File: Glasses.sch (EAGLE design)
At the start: 7 parts, among them U1 APA1022020, U2 APA1022020, U3 APA1022020, U4 APA1022020, U5 APA1022020, U6 APA1022020

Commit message: laid out LED's
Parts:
- added FRAME2, FRAME3, FRAME4, FRAME5, FRAME6, FRAME7: FRAME-LETTERNO_PACKAGE, SparkFun-Aesthetics:FRAME-LETTERNO_PACKAGE
- added U10, U100, U101, U102, U103, U104, U105, U106, U107, U108, U109, U11, U110, U111, U112, U113, U114, U115, U116, U117, U118, U119, U12, U120, U121, U122, U123, U124, U125, U126, U127, U128, U129, U13, U130, U131, U132, U133, U134, U135, U136, U137, U138, U139, U14, U140, U141, U142, U143, U144, U145, U146, U147, U148, U149, U15, U150, U151, U152, U153, U154, U155, U156, U157, U158, U159, U16, U160, U161, U162, U163, U164, U165, U166, U167, U168, U169, U17, U170, U171, U172, U173, U174, U175, U176, U177, U178, U179, U18, U180, U181, U182, U183, U184, U185, U186, U187, U188, U189, U19, U190, U20, U21, U22, U23, U24, U25, U26, U27, U28, U29, U30, U31, U32, U33, U34, U35, U36, U37, U38, U39, U40, U41, U42, U43, U44, U45, U46, U47, U48, U49, U50, U51, U52, U53, U54, U55, U56, U57, U58, U59, U60, U61, U62, U63, U64, U65, U66, U67, U68, U69, U7, U70, U71, U72, U73, U74, U75, U76, U77, U78, U79, U8, U80, U81, U82, U83, U84, U85, U86, U87, U88, U89, U9, U90, U91, U92, U93, U94, U95, U96, U97, U98, U99: APA1022020, 1_BES_Optoelectronics:APA1022020
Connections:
- new net CK1: U28.CO, U29.CI
- new net CK2: U56.CO, U57.CI
- new net CK3: U84.CO, U85.CI
- new net CK4: U112.CO, U113.CI
- new net CK5: U140.CO, U141.CI
- new net CK6: U168.CO, U169.CI
- new net N$100: U53.DO, U54.DI
- new net N$101: U54.CO, U55.CI
- new net N$102: U54.DO, U55.DI
- new net N$103: U55.CO, U56.CI
- new net N$104: U55.DO, U56.DI
- new net N$105: U49.DO, U50.DI
- new net N$106: U49.CO, U50.CI
- new net N$107: U42.DO, U43.DI
- new net N$108: U42.CO, U43.CI
- new net N$109: U57.DO, U58.DI
- new net N$11: U6.CO, U7.CI
- new net N$110: U57.CO, U58.CI
- new net N$111: U58.CO, U59.CI
- new net N$112: U58.DO, U59.DI
- new net N$113: U59.DO, U60.DI
- new net N$114: U59.CO, U60.CI
- new net N$115: U60.CO, U61.CI
- new net N$116: U60.DO, U61.DI
- new net N$117: U61.CO, U62.CI
- new net N$118: U61.DO, U62.DI
- new net N$119: U62.CO, U63.CI
- new net N$12: U6.DO, U7.DI
- new net N$120: U62.DO, U63.DI
- new net N$121: U64.DO, U65.DI
- new net N$122: U64.CO, U65.CI
- new net N$123: U65.CO, U66.CI
- new net N$124: U65.DO, U66.DI
- new net N$125: U66.DO, U67.DI
- new net N$126: U66.CO, U67.CI
- new net N$127: U67.CO, U68.CI
- new net N$128: U67.DO, U68.DI
- new net N$129: U68.CO, U69.CI
- new net N$13: U8.DO, U9.DI
- new net N$130: U68.DO, U69.DI
- new net N$131: U69.CO, U70.CI
- new net N$132: U69.DO, U70.DI
- new net N$133: U63.DO, U64.DI
- new net N$134: U63.CO, U64.CI
- new net N$135: U71.DO, U72.DI
- new net N$136: U71.CO, U72.CI
- new net N$137: U72.CO, U73.CI
- new net N$138: U72.DO, U73.DI
- new net N$139: U73.DO, U74.DI
- new net N$14: U8.CO, U9.CI
- new net N$140: U73.CO, U74.CI
- new net N$141: U74.CO, U75.CI
- new net N$142: U74.DO, U75.DI
- new net N$143: U75.CO, U76.CI
- new net N$144: U75.DO, U76.DI
- new net N$145: U76.CO, U77.CI
- new net N$146: U76.DO, U77.DI
- new net N$147: U78.DO, U79.DI
- new net N$148: U78.CO, U79.CI
- new net N$149: U79.CO, U80.CI
- new net N$15: U10.CI, U9.CO
- new net N$150: U79.DO, U80.DI
- new net N$151: U80.DO, U81.DI
- new net N$152: U80.CO, U81.CI
- new net N$153: U81.CO, U82.CI
- new net N$154: U81.DO, U82.DI
- new net N$155: U82.CO, U83.CI
- new net N$156: U82.DO, U83.DI
- new net N$157: U83.CO, U84.CI
- new net N$158: U83.DO, U84.DI
- new net N$159: U77.DO, U78.DI
- new net N$16: U10.DI, U9.DO
- new net N$160: U77.CO, U78.CI
- new net N$161: U70.DO, U71.DI
- new net N$162: U70.CO, U71.CI
- new net N$163: U85.DO, U86.DI
- new net N$164: U85.CO, U86.CI
- new net N$165: U86.CO, U87.CI
- new net N$166: U86.DO, U87.DI
- new net N$167: U87.DO, U88.DI
- new net N$168: U87.CO, U88.CI
- new net N$169: U88.CO, U89.CI
- new net N$17: U10.DO, U11.DI
- new net N$170: U88.DO, U89.DI
- new net N$171: U89.CO, U90.CI
- new net N$172: U89.DO, U90.DI
- new net N$173: U90.CO, U91.CI
- new net N$174: U90.DO, U91.DI
- new net N$175: U92.DO, U93.DI
- new net N$176: U92.CO, U93.CI
- new net N$177: U93.CO, U94.CI
- new net N$178: U93.DO, U94.DI
- new net N$179: U94.DO, U95.DI
- new net N$18: U10.CO, U11.CI
- new net N$180: U94.CO, U95.CI
- new net N$183: U96.CO, U97.CI
- new net N$184: U96.DO, U97.DI
- new net N$185: U97.CO, U98.CI
- new net N$186: U97.DO, U98.DI
- new net N$187: U91.DO, U92.DI
- new net N$188: U91.CO, U92.CI
- new net N$189: U100.DI, U99.DO
- new net N$19: U11.CO, U12.CI
- new net N$190: U100.CI, U99.CO
- new net N$191: U100.CO, U101.CI
- new net N$192: U100.DO, U101.DI
- new net N$193: U101.DO, U102.DI
- new net N$194: U101.CO, U102.CI
- new net N$195: U102.CO, U103.CI
- new net N$196: U102.DO, U103.DI
- new net N$197: U103.CO, U104.CI
- new net N$198: U103.DO, U104.DI
- new net N$199: U104.CO, U105.CI
- new net N$20: U11.DO, U12.DI
- new net N$200: U104.DO, U105.DI
- new net N$201: U106.DO, U107.DI
- new net N$202: U106.CO, U107.CI
- new net N$203: U107.CO, U108.CI
- new net N$204: U107.DO, U108.DI
- new net N$205: U108.DO, U109.DI
- new net N$206: U108.CO, U109.CI
- new net N$207: U109.CO, U110.CI
- new net N$208: U109.DO, U110.DI
- new net N$209: U110.CO, U111.CI
- new net N$21: U12.CO, U13.CI
- new net N$210: U110.DO, U111.DI
- new net N$211: U111.CO, U112.CI
- new net N$212: U111.DO, U112.DI
- new net N$213: U105.DO, U106.DI
- new net N$214: U105.CO, U106.CI
- new net N$215: U98.DO, U99.DI
- new net N$216: U98.CO, U99.CI
- new net N$217: U113.DO, U114.DI
- new net N$218: U113.CO, U114.CI
- new net N$219: U114.CO, U115.CI
- new net N$22: U12.DO, U13.DI
- new net N$220: U114.DO, U115.DI
- new net N$221: U115.DO, U116.DI
- new net N$222: U115.CO, U116.CI
- new net N$223: U116.CO, U117.CI
- new net N$224: U116.DO, U117.DI
- new net N$225: U117.CO, U118.CI
- new net N$226: U117.DO, U118.DI
- new net N$227: U118.CO, U119.CI
- new net N$228: U118.DO, U119.DI
- new net N$229: U120.DO, U121.DI
- new net N$23: U13.CO, U14.CI
- new net N$230: U120.CO, U121.CI
- new net N$231: U121.CO, U122.CI
- new net N$232: U121.DO, U122.DI
- new net N$233: U122.DO, U123.DI
- new net N$234: U122.CO, U123.CI
- new net N$235: U123.CO, U124.CI
- new net N$236: U123.DO, U124.DI
- new net N$237: U124.CO, U125.CI
- new net N$238: U124.DO, U125.DI
- new net N$239: U125.CO, U126.CI
- new net N$24: U13.DO, U14.DI
- new net N$240: U125.DO, U126.DI
- new net N$241: U119.DO, U120.DI
- new net N$242: U119.CO, U120.CI
- new net N$243: U127.DO, U128.DI
- new net N$244: U127.CO, U128.CI
- new net N$245: U128.CO, U129.CI
- new net N$246: U128.DO, U129.DI
- new net N$247: U129.DO, U130.DI
- new net N$248: U129.CO, U130.CI
- new net N$249: U130.CO, U131.CI
- new net N$25: U7.DO, U8.DI
- new net N$250: U130.DO, U131.DI
- new net N$251: U131.CO, U132.CI
- new net N$252: U131.DO, U132.DI
- new net N$253: U132.CO, U133.CI
- new net N$254: U132.DO, U133.DI
- new net N$255: U134.DO, U135.DI
- new net N$256: U134.CO, U135.CI
- new net N$257: U135.CO, U136.CI
- new net N$258: U135.DO, U136.DI
- new net N$259: U136.DO, U137.DI
- new net N$26: U7.CO, U8.CI
- new net N$260: U136.CO, U137.CI
- new net N$261: U137.CO, U138.CI
- new net N$262: U137.DO, U138.DI
- new net N$263: U138.CO, U139.CI
- new net N$264: U138.DO, U139.DI
- new net N$265: U139.CO, U140.CI
- new net N$266: U139.DO, U140.DI
- new net N$267: U133.DO, U134.DI
- new net N$268: U133.CO, U134.CI
- new net N$269: U126.DO, U127.DI
- new net N$27: U15.DO, U16.DI
- new net N$270: U126.CO, U127.CI
- new net N$271: U141.DO, U142.DI
- new net N$272: U141.CO, U142.CI
- new net N$273: U142.CO, U143.CI
- new net N$274: U142.DO, U143.DI
- new net N$275: U143.DO, U144.DI
- new net N$276: U143.CO, U144.CI
- new net N$277: U144.CO, U145.CI
- new net N$278: U144.DO, U145.DI
- new net N$279: U145.CO, U146.CI
- new net N$28: U15.CO, U16.CI
- new net N$280: U145.DO, U146.DI
- new net N$281: U146.CO, U147.CI
- new net N$282: U146.DO, U147.DI
- new net N$283: U148.DO, U149.DI
- new net N$284: U148.CO, U149.CI
- new net N$285: U149.CO, U150.CI
- new net N$286: U149.DO, U150.DI
- new net N$287: U150.DO, U151.DI
- new net N$288: U150.CO, U151.CI
- new net N$289: U151.CO, U152.CI
- new net N$29: U16.CO, U17.CI
- new net N$290: U151.DO, U152.DI
- new net N$291: U152.CO, U153.CI
- new net N$292: U152.DO, U153.DI
- new net N$293: U153.CO, U154.CI
- new net N$294: U153.DO, U154.DI
- new net N$295: U147.DO, U148.DI
- new net N$296: U147.CO, U148.CI
- new net N$297: U155.DO, U156.DI
- new net N$298: U155.CO, U156.CI
- new net N$299: U156.CO, U157.CI
- new net N$30: U16.DO, U17.DI
- new net N$300: U156.DO, U157.DI
- new net N$301: U157.DO, U158.DI
- new net N$302: U157.CO, U158.CI
- new net N$303: U158.CO, U159.CI
- new net N$304: U158.DO, U159.DI
- new net N$305: U159.CO, U160.CI
- new net N$306: U159.DO, U160.DI
- new net N$307: U160.CO, U161.CI
- new net N$308: U160.DO, U161.DI
- new net N$309: U162.DO, U163.DI
- new net N$31: U17.DO, U18.DI
- new net N$310: U162.CO, U163.CI
- new net N$311: U163.CO, U164.CI
- new net N$312: U163.DO, U164.DI
- new net N$313: U164.DO, U165.DI
- new net N$314: U164.CO, U165.CI
- new net N$315: U165.CO, U166.CI
- new net N$316: U165.DO, U166.DI
- new net N$317: U166.CO, U167.CI
- new net N$318: U166.DO, U167.DI
- new net N$319: U167.CO, U168.CI
- new net N$32: U17.CO, U18.CI
- new net N$320: U167.DO, U168.DI
- new net N$321: U161.DO, U162.DI
- new net N$322: U161.CO, U162.CI
- new net N$323: U154.DO, U155.DI
- new net N$324: U154.CO, U155.CI
- new net N$325: U169.DO, U170.DI
- new net N$326: U169.CO, U170.CI
- new net N$327: U170.CO, U171.CI
- new net N$328: U170.DO, U171.DI
- new net N$329: U171.DO, U172.DI
- new net N$33: U18.CO, U19.CI
- new net N$330: U171.CO, U172.CI
- new net N$331: U172.CO, U173.CI
- new net N$332: U172.DO, U173.DI
- new net N$333: U173.CO, U174.CI
- new net N$334: U173.DO, U174.DI
- new net N$335: U174.CO, U175.CI
- new net N$336: U174.DO, U175.DI
- new net N$337: U176.DO, U177.DI
- new net N$338: U176.CO, U177.CI
- new net N$339: U177.CO, U178.CI
- new net N$34: U18.DO, U19.DI
- new net N$340: U177.DO, U178.DI
- new net N$341: U178.DO, U179.DI
- new net N$342: U178.CO, U179.CI
- new net N$343: U179.CO, U180.CI
- new net N$344: U179.DO, U180.DI
- new net N$345: U180.CO, U181.CI
- new net N$346: U180.DO, U181.DI
- new net N$347: U181.CO, U182.CI
- new net N$348: U181.DO, U182.DI
- new net N$349: U175.DO, U176.DI
- new net N$35: U19.CO, U20.CI
- new net N$350: U175.CO, U176.CI
- new net N$351: U183.DO, U184.DI
- new net N$352: U183.CO, U184.CI
- new net N$353: U184.CO, U185.CI
- new net N$354: U184.DO, U185.DI
- new net N$355: U185.DO, U186.DI
- new net N$356: U185.CO, U186.CI
- new net N$357: U186.CO, U187.CI
- new net N$358: U186.DO, U187.DI
- new net N$359: U187.CO, U188.CI
- new net N$36: U19.DO, U20.DI
- new net N$360: U187.DO, U188.DI
- new net N$361: U188.CO, U189.CI
- new net N$362: U188.DO, U189.DI
- new net N$37: U20.CO, U21.CI
- new net N$375: U189.DO, U190.DI
- new net N$376: U189.CO, U190.CI
- new net N$377: U182.DO, U183.DI
- new net N$378: U182.CO, U183.CI
- new net N$38: U20.DO, U21.DI
- new net N$39: U22.DO, U23.DI
- new net N$40: U22.CO, U23.CI
- new net N$41: U23.CO, U24.CI
- new net N$42: U23.DO, U24.DI
- new net N$43: U24.DO, U25.DI
- new net N$44: U24.CO, U25.CI
- new net N$45: U25.CO, U26.CI
- new net N$46: U25.DO, U26.DI
- new net N$47: U26.CO, U27.CI
- new net N$48: U26.DO, U27.DI
- new net N$49: U27.CO, U28.CI
- new net N$50: U27.DO, U28.DI
- new net N$51: U21.DO, U22.DI
- new net N$52: U21.CO, U22.CI
- new net N$53: U14.DO, U15.DI
- new net N$54: U14.CO, U15.CI
- new net N$55: U29.DO, U30.DI
- new net N$56: U29.CO, U30.CI
- new net N$57: U30.CO, U31.CI
- new net N$58: U30.DO, U31.DI
- new net N$59: U31.DO, U32.DI
- new net N$60: U31.CO, U32.CI
- new net N$61: U32.CO, U33.CI
- new net N$62: U32.DO, U33.DI
- new net N$63: U33.CO, U34.CI
- new net N$64: U33.DO, U34.DI
- new net N$65: U34.CO, U35.CI
- new net N$66: U34.DO, U35.DI
- new net N$67: U36.DO, U37.DI
- new net N$68: U36.CO, U37.CI
- new net N$69: U37.CO, U38.CI
- new net N$70: U37.DO, U38.DI
- new net N$71: U38.DO, U39.DI
- new net N$72: U38.CO, U39.CI
- new net N$73: U39.CO, U40.CI
- new net N$74: U39.DO, U40.DI
- new net N$75: U40.CO, U41.CI
- new net N$76: U40.DO, U41.DI
- new net N$77: U41.CO, U42.CI
- new net N$78: U41.DO, U42.DI
- new net N$79: U35.DO, U36.DI
- new net N$80: U35.CO, U36.CI
- new net N$81: U43.DO, U44.DI
- new net N$82: U43.CO, U44.CI
- new net N$83: U44.CO, U45.CI
- new net N$84: U44.DO, U45.DI
- new net N$85: U45.DO, U46.DI
- new net N$86: U45.CO, U46.CI
- new net N$87: U46.CO, U47.CI
- new net N$88: U46.DO, U47.DI
- new net N$89: U47.CO, U48.CI
- new net N$90: U47.DO, U48.DI
- new net N$91: U48.CO, U49.CI
- new net N$92: U48.DO, U49.DI
- new net N$93: U50.DO, U51.DI
- new net N$94: U50.CO, U51.CI
- new net N$95: U51.CO, U52.CI
- new net N$96: U51.DO, U52.DI
- new net N$97: U52.DO, U53.DI
- new net N$98: U52.CO, U53.CI
- new net N$99: U53.CO, U54.CI
- new net SD1: U28.DO, U29.DI
- new net SD2: U56.DO, U57.DI
- new net SD3: U84.DO, U85.DI
- new net SD4: U112.DO, U113.DI
- new net SD5: U140.DO, U141.DI
- new net SD6: U168.DO, U169.DI
- net GND: now also U10.GND, U100.GND, U101.GND, U102.GND, U103.GND, U104.GND, U105.GND, U106.GND, U107.GND, U108.GND, U109.GND, U11.GND, U110.GND, U111.GND, U112.GND, U113.GND, U114.GND, U115.GND, U116.GND, U117.GND, U118.GND, U119.GND, U12.GND, U120.GND, U121.GND, U122.GND, U123.GND, U124.GND, U125.GND, U126.GND, U127.GND, U128.GND, U129.GND, U13.GND, U130.GND, U131.GND, U132.GND, U133.GND, U134.GND, U135.GND, U136.GND, U137.GND, U138.GND, U139.GND, U14.GND, U140.GND, U141.GND, U142.GND, U143.GND, U144.GND, U145.GND, U146.GND, U147.GND, U148.GND, U149.GND, U15.GND, U150.GND, U151.GND, U152.GND, U153.GND, U154.GND, U155.GND, U156.GND, U157.GND, U158.GND, U159.GND, U16.GND, U160.GND, U161.GND, U162.GND, U163.GND, U164.GND, U165.GND, U166.GND, U167.GND, U168.GND, U169.GND, U17.GND, U170.GND, U171.GND, U172.GND, U173.GND, U174.GND, U175.GND, U176.GND, U177.GND, U178.GND, U179.GND, U18.GND, U180.GND, U181.GND, U182.GND, U183.GND, U184.GND, U185.GND, U186.GND, U187.GND, U188.GND, U189.GND, U19.GND, U190.GND, U20.GND, U21.GND, U22.GND, U23.GND, U24.GND, U25.GND, U26.GND, U27.GND, U28.GND, U29.GND, U30.GND, U31.GND, U32.GND, U33.GND, U34.GND, U35.GND, U36.GND, U37.GND, U38.GND, U39.GND, U40.GND, U41.GND, U42.GND, U43.GND, U44.GND, U45.GND, U46.GND, U47.GND, U48.GND, U49.GND, U50.GND, U51.GND, U52.GND, U53.GND, U54.GND, U55.GND, U56.GND, U57.GND, U58.GND, U59.GND, U60.GND, U61.GND, U62.GND, U63.GND, U64.GND, U65.GND, U66.GND, U67.GND, U68.GND, U69.GND, U7.GND, U70.GND, U71.GND, U72.GND, U73.GND, U74.GND, U75.GND, U76.GND, U77.GND, U78.GND, U79.GND, U8.GND, U80.GND, U81.GND, U82.GND, U83.GND, U84.GND, U85.GND, U86.GND, U87.GND, U88.GND, U89.GND, U9.GND, U90.GND, U91.GND, U92.GND, U93.GND, U94.GND, U95.GND, U96.GND, U97.GND, U98.GND, U99.GND
- net VCC: now also U10.VCC, U100.VCC, U101.VCC, U102.VCC, U103.VCC, U104.VCC, U105.VCC, U106.VCC, U107.VCC, U108.VCC, U109.VCC, U11.VCC, U110.VCC, U111.VCC, U112.VCC, U113.VCC, U114.VCC, U115.VCC, U116.VCC, U117.VCC, U118.VCC, U119.VCC, U12.VCC, U120.VCC, U121.VCC, U122.VCC, U123.VCC, U124.VCC, U125.VCC, U126.VCC, U127.VCC, U128.VCC, U129.VCC, U13.VCC, U130.VCC, U131.VCC, U132.VCC, U133.VCC, U134.VCC, U135.VCC, U136.VCC, U137.VCC, U138.VCC, U139.VCC, U14.VCC, U140.VCC, U141.VCC, U142.VCC, U143.VCC, U144.VCC, U145.VCC, U146.VCC, U147.VCC, U148.VCC, U149.VCC, U15.VCC, U150.VCC, U151.VCC, U152.VCC, U153.VCC, U154.VCC, U155.VCC, U156.VCC, U157.VCC, U158.VCC, U159.VCC, U16.VCC, U160.VCC, U161.VCC, U162.VCC, U163.VCC, U164.VCC, U165.VCC, U166.VCC, U167.VCC, U168.VCC, U169.VCC, U17.VCC, U170.VCC, U171.VCC, U172.VCC, U173.VCC, U174.VCC, U175.VCC, U176.VCC, U177.VCC, U178.VCC, U179.VCC, U18.VCC, U180.VCC, U181.VCC, U182.VCC, U183.VCC, U184.VCC, U185.VCC, U186.VCC, U187.VCC, U188.VCC, U189.VCC, U19.VCC, U190.VCC, U20.VCC, U21.VCC, U22.VCC, U23.VCC, U24.VCC, U25.VCC, U26.VCC, U27.VCC, U28.VCC, U29.VCC, U30.VCC, U31.VCC, U32.VCC, U33.VCC, U34.VCC, U35.VCC, U36.VCC, U37.VCC, U38.VCC, U39.VCC, U40.VCC, U41.VCC, U42.VCC, U43.VCC, U44.VCC, U45.VCC, U46.VCC, U47.VCC, U48.VCC, U49.VCC, U50.VCC, U51.VCC, U52.VCC, U53.VCC, U54.VCC, U55.VCC, U56.VCC, U57.VCC, U58.VCC, U59.VCC, U60.VCC, U61.VCC, U62.VCC, U63.VCC, U64.VCC, U65.VCC, U66.VCC, U67.VCC, U68.VCC, U69.VCC, U7.VCC, U70.VCC, U71.VCC, U72.VCC, U73.VCC, U74.VCC, U75.VCC, U76.VCC, U77.VCC, U78.VCC, U79.VCC, U8.VCC, U80.VCC, U81.VCC, U82.VCC, U83.VCC, U84.VCC, U85.VCC, U86.VCC, U87.VCC, U88.VCC, U89.VCC, U9.VCC, U90.VCC, U91.VCC, U92.VCC, U93.VCC, U94.VCC, U95.VCC, U96.VCC, U97.VCC, U98.VCC, U99.VCC

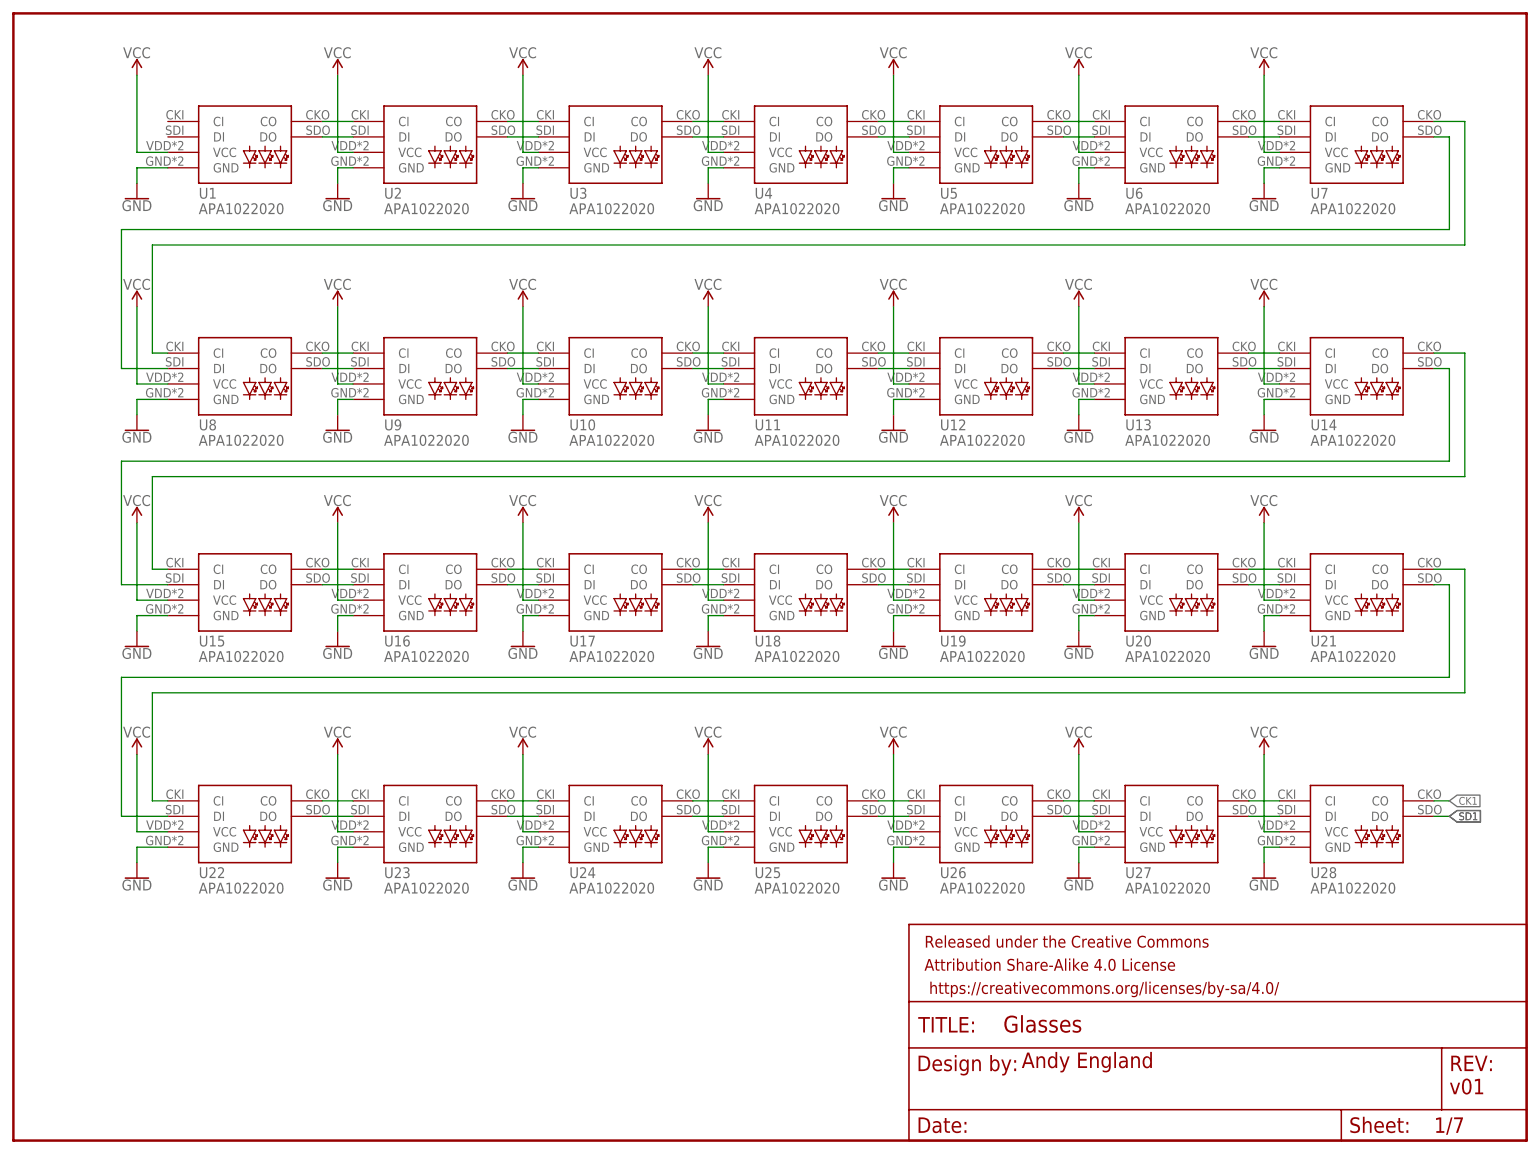
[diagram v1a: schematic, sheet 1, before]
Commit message: changed diameter, began LED layout
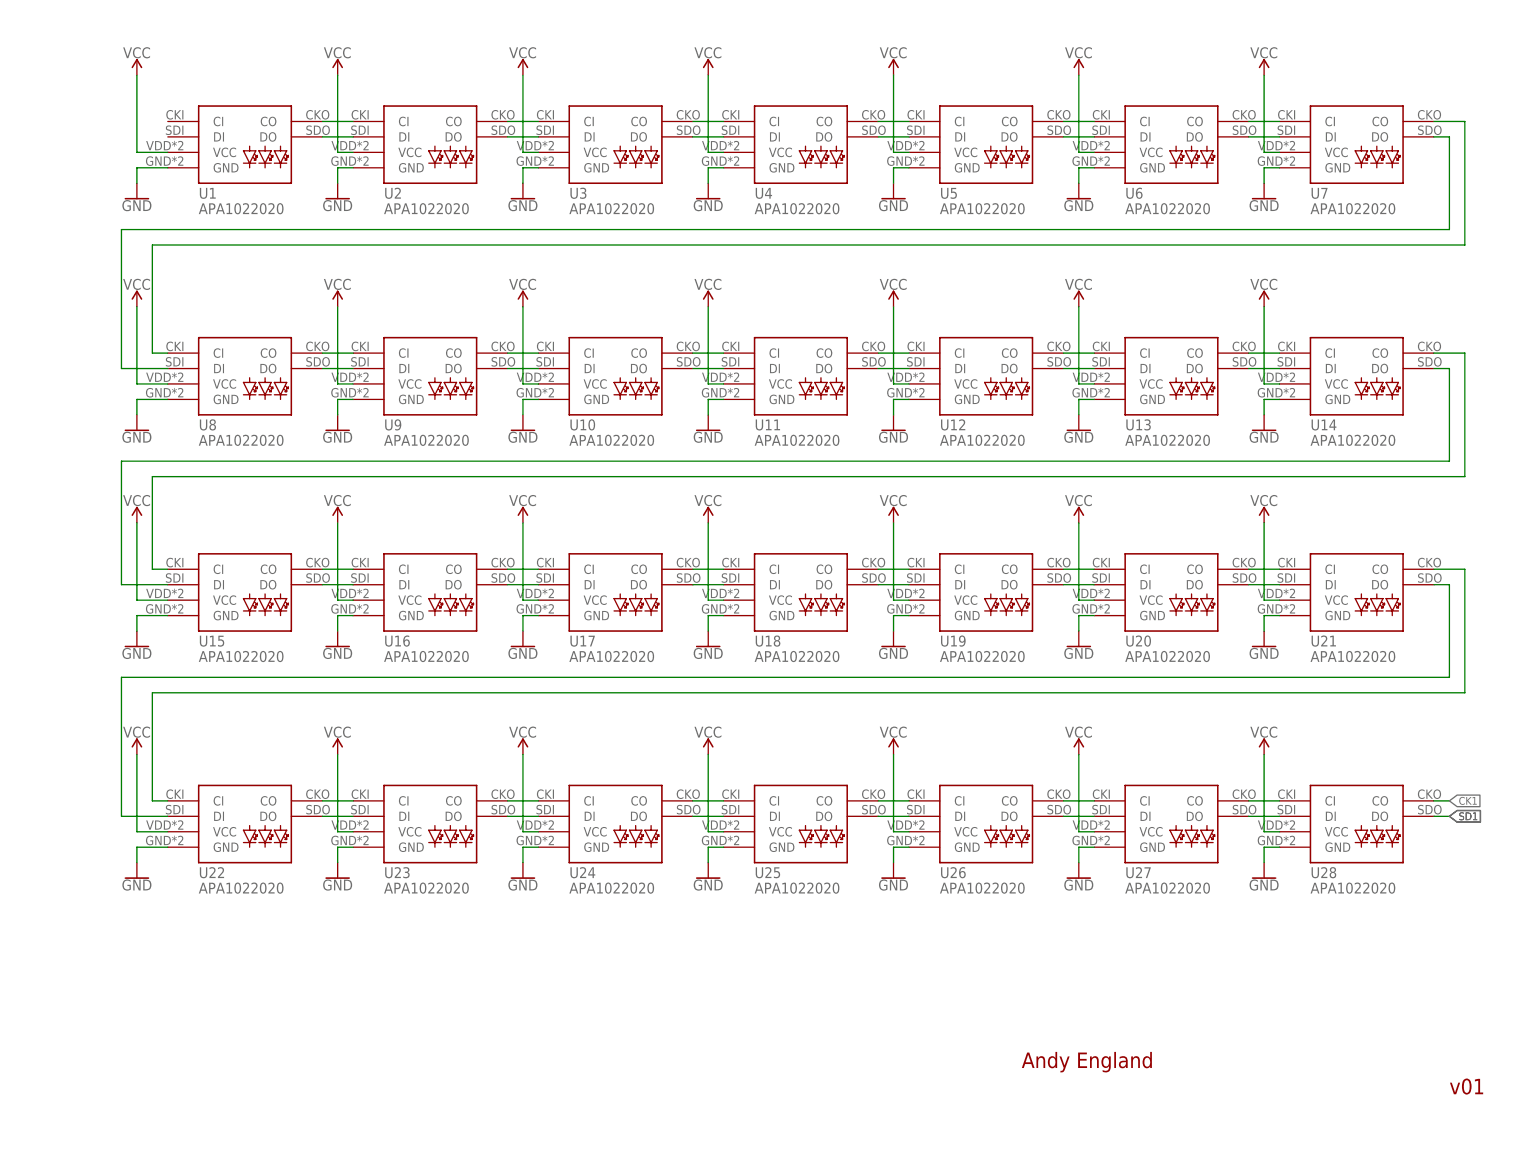
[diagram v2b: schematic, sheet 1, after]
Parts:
- removed FRAME1, FRAME2, FRAME3, FRAME4, FRAME5, FRAME6, FRAME7: FRAME-LETTERNO_PACKAGE, SparkFun-Aesthetics:FRAME-LETTERNO_PACKAGE
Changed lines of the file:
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@@
 </classes>
 <parts>
-<part name="FRAME1" library="SparkFun-Aesthetics" deviceset="FRAME-LETTER" device="NO_PACKAGE"/>
 <part name="U1" library="1_BES_Optoelectronics" deviceset="APA102" device="2020"/>
 <part name="SUPPLY1" library="SparkFun-PowerSymbols" deviceset="VCC" device=""/>
@@
 <part name="SUPPLY56" library="SparkFun-PowerSymbols" deviceset="VCC" device=""/>
 <part name="GND56" library="SparkFun-PowerSymbols" deviceset="GND" device=""/>
-<part name="FRAME2" library="SparkFun-Aesthetics" deviceset="FRAME-LETTER" device="NO_PACKAGE"/>
 <part name="U57" library="1_BES_Optoelectronics" deviceset="APA102" device="2020"/>
 <part name="SUPPLY57" library="SparkFun-PowerSymbols" deviceset="VCC" device=""/>
@@
 <part name="SUPPLY84" library="SparkFun-PowerSymbols" deviceset="VCC" device=""/>
 <part name="GND84" library="SparkFun-PowerSymbols" deviceset="GND" device=""/>
-<part name="FRAME3" library="SparkFun-Aesthetics" deviceset="FRAME-LETTER" device="NO_PACKAGE"/>
 <part name="U85" library="1_BES_Optoelectronics" deviceset="APA102" device="2020"/>
 <part name="SUPPLY85" library="SparkFun-PowerSymbols" deviceset="VCC" device=""/>
@@
 <part name="SUPPLY112" library="SparkFun-PowerSymbols" deviceset="VCC" device=""/>
 <part name="GND112" library="SparkFun-PowerSymbols" deviceset="GND" device=""/>
-<part name="FRAME4" library="SparkFun-Aesthetics" deviceset="FRAME-LETTER" device="NO_PACKAGE"/>
 <part name="U113" library="1_BES_Optoelectronics" deviceset="APA102" device="2020"/>
 <part name="SUPPLY113" library="SparkFun-PowerSymbols" deviceset="VCC" device=""/>
@@
 <part name="SUPPLY140" library="SparkFun-PowerSymbols" deviceset="VCC" device=""/>
 <part name="GND140" library="SparkFun-PowerSymbols" deviceset="GND" device=""/>
-<part name="FRAME5" library="SparkFun-Aesthetics" deviceset="FRAME-LETTER" device="NO_PACKAGE"/>
 <part name="U141" library="1_BES_Optoelectronics" deviceset="APA102" device="2020"/>
 <part name="SUPPLY141" library="SparkFun-PowerSymbols" deviceset="VCC" device=""/>
@@
 <part name="SUPPLY168" library="SparkFun-PowerSymbols" deviceset="VCC" device=""/>
 <part name="GND168" library="SparkFun-PowerSymbols" deviceset="GND" device=""/>
-<part name="FRAME6" library="SparkFun-Aesthetics" deviceset="FRAME-LETTER" device="NO_PACKAGE"/>
 <part name="U169" library="1_BES_Optoelectronics" deviceset="APA102" device="2020"/>
 <part name="SUPPLY169" library="SparkFun-PowerSymbols" deviceset="VCC" device=""/>
@@
 <part name="SUPPLY190" library="SparkFun-PowerSymbols" deviceset="VCC" device=""/>
 <part name="GND190" library="SparkFun-PowerSymbols" deviceset="GND" device=""/>
-<part name="FRAME7" library="SparkFun-Aesthetics" deviceset="FRAME-LETTER" device="NO_PACKAGE"/>
 </parts>
 <sheets>
@@
 </plain>
 <instances>
-<instance part="FRAME1" gate="G$1" x="0" y="0"/>
-<instance part="FRAME1" gate="V" x="147.32" y="0"/>
 <instance part="U1" gate="G$1" x="38.1" y="162.56"/>
 <instance part="SUPPLY1" gate="G$1" x="20.32" y="175.26"/>
@@
 <instance part="SUPPLY56" gate="G$1" x="205.74" y="63.5"/>
 <instance part="GND56" gate="1" x="205.74" y="43.18"/>
-<instance part="FRAME2" gate="G$1" x="0" y="0"/>
-<instance part="FRAME2" gate="V" x="147.32" y="0"/>
 </instances>
 <busses>
@@
 <instance part="SUPPLY84" gate="G$1" x="205.74" y="63.5"/>
 <instance part="GND84" gate="1" x="205.74" y="43.18"/>
-<instance part="FRAME3" gate="G$1" x="0" y="0"/>
-<instance part="FRAME3" gate="V" x="147.32" y="0"/>
 </instances>
 <busses>
@@
 <instance part="SUPPLY112" gate="G$1" x="205.74" y="63.5"/>
 <instance part="GND112" gate="1" x="205.74" y="43.18"/>
-<instance part="FRAME4" gate="G$1" x="0" y="0"/>
-<instance part="FRAME4" gate="V" x="147.32" y="0"/>
 </instances>
 <busses>
@@
 <instance part="SUPPLY140" gate="G$1" x="205.74" y="63.5"/>
 <instance part="GND140" gate="1" x="205.74" y="43.18"/>
-<instance part="FRAME5" gate="G$1" x="0" y="0"/>
-<instance part="FRAME5" gate="V" x="147.32" y="0"/>
 </instances>
 <busses>
@@
 <instance part="SUPPLY168" gate="G$1" x="205.74" y="63.5"/>
 <instance part="GND168" gate="1" x="205.74" y="43.18"/>
-<instance part="FRAME6" gate="G$1" x="0" y="0"/>
-<instance part="FRAME6" gate="V" x="147.32" y="0"/>
 </instances>
 <busses>
@@
 <instance part="SUPPLY190" gate="G$1" x="20.32" y="63.5"/>
 <instance part="GND190" gate="1" x="20.32" y="43.18"/>
-<instance part="FRAME7" gate="G$1" x="0" y="0"/>
-<instance part="FRAME7" gate="V" x="147.32" y="0"/>
 </instances>
 <busses>
